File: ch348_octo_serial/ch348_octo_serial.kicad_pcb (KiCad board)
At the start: 2 copper layers, 88.9 x 88.9 mm, 73 parts, among them J1 USB_C_Receptacle_USB2.0, J10 Conn_01x07, J11 JLCPCB_3.5MM_SOCKET_C18166, J12 Conn_01x07, J13 JLCPCB_3.5MM_SOCKET_C18166, J14 Conn_01x07, J15 JLCPCB_3.5MM_SOCKET_C18166, J16 Conn_01x07, J17 JLCPCB_3.5MM_SOCKET_C18166, J18 Conn_01x07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

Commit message: ch348_octo_serial: fully routed, silk pending
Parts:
- moved D3 5.84 mm to (70.4, 80.0)
- moved D4 5.84 mm to (70.4, 87.6)
- moved R14 5.84 mm to (72.9, 80.0)
- moved R15 5.84 mm to (72.9, 87.6)
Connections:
- net Net-(C7-Pad1) renamed /RESET
- net Net-(C8-Pad1) renamed /XI
- net Net-(C9-Pad1) renamed /XO
- net Net-(D2-Pad1) renamed /ACT
- net Net-(R12-Pad2) renamed /TEST
- net Net-(R13-Pad2) renamed /CFG
- net Net-(R14-Pad1) renamed /RX_S
- net Net-(R15-Pad1) renamed /TX_S
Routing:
- net Vdrive: track 0.00 -> 533.0 mm, vias 0 -> 4
- net +3.3V: track 0.00 -> 198.4 mm, vias 0 -> 10
- net +5V: track 0.00 -> 135.3 mm, vias 0 -> 5
- net /Serial Connector 0/RTS: track 0.00 -> 86.6 mm, vias 0 -> 2
- net /Serial Connector 0/DTR: track 0.00 -> 86.1 mm, vias 0 -> 1
- net /Serial Connector 2/DTR: track 0.00 -> 84.9 mm, vias 0 -> 1
- net /Serial Connector 0/RXD: track 0.00 -> 81.9 mm, vias 0 -> 1
- net /Serial Connector 0/CTS: track 0.00 -> 80.3 mm, vias 0 -> 1
- net /Serial Connector 0/TXD: track 0.00 -> 77.8 mm, vias 0 -> 1
- net /Serial Connector 3/RXD: track 0.00 -> 70.9 mm, vias 0 -> 1
- net /Serial Connector 1/CTS: track 0.00 -> 70.4 mm, vias 0 -> 3
- net /Serial Connector 6/DTR: track 0.00 -> 68.5 mm, vias 0 -> 4
- net /Serial Connector 4/DTR: track 0.00 -> 67.7 mm, vias 0 -> 3
- net /Serial Connector 6/RTS: track 0.00 -> 67.1 mm
- net /Serial Connector 5/RXD: track 0.00 -> 65.9 mm, vias 0 -> 2
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- added copper zone on In2.Cu, net GND
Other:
- copper layers 2 -> 4

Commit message: ch348_octo_serial: Dec2022 as submitted
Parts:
- added H1: Front Octopus, ch348_octo_serial:octopus, F.Cu at (110.7, 75.7)
- added H2: Back Octopus, ch348_octo_serial:octopus_120, B.Cu at (107.6, 87.5)
- moved C1 16.8 mm to (94.5, 89.0), turned to 0 degrees
- moved R2 16.8 mm to (97.9, 88.6)
- moved R3 16.8 mm to (99.2, 88.6)
- moved VR1 16.8 mm to (96.1, 94.2)
- moved C4 16.7 mm to (92.2, 97.5), turned to 180 degrees
- moved J2 9.90 mm to (140.3, 56.5)
- moved J3 9.90 mm to (85.7, 56.5)
- moved J4 9.90 mm to (140.3, 111.1)
- moved J5 9.90 mm to (85.7, 111.1)
- moved C16 6.92 mm to (114.0, 107.1), turned to -90 degrees
- moved C22 5.32 mm to (71.5, 65.0), turned to 180 degrees
- moved C20 4.99 mm to (130.8, 45.0)
- moved C18 4.89 mm to (153.2, 102.4), turned to 0 degrees
- moved C24 4.44 mm to (94.2, 124.2), turned to -90 degrees
- moved R16 2.05 mm to (108.5, 118.4), turned to 180 degrees
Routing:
- net +3.3V: track 198.4 -> 189.3 mm
- net Vdrive: track 533.0 -> 541.7 mm
- net +5V: track 135.3 -> 128.6 mm
- net /Serial Connector 0/CTS: track 80.3 -> 76.9 mm
- net /Serial Connector 0/TXD: track 77.8 -> 79.7 mm
- net GND: track 64.1 -> 65.5 mm
- net /Serial Connector 0/RTS: track 86.6 -> 87.9 mm
- net /Serial Connector 1/TXD: track 57.9 -> 56.6 mm
- net /Serial Connector 0/RXD: track 81.9 -> 83.0 mm
- net /Serial Connector 6/CTS: track 56.4 -> 55.6 mm
- net /Serial Connector 1/CTS: track 70.4 -> 69.6 mm
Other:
- board text added: "+VIN-"
- board text added: "0"
- board text added: "1"
- board text added: "1.8V"
- board text added: "2"
- board text added: "2.5V"
- board text added: "3"
- board text added: "3.3V"
- board text added: "4"
- board text added: "5"
- board text added: "6"
- board text added: "7"
- board text added: "ACT"
- board text added: "CTS"
- board text added: "DTR"
- board text added: "GND"
- board text added: "RTS"
- board text added: "RX<"
- board text added: "RXD<"
- board text added: "TX>"
- board text added: "TXD>"
- board text added: "VCC"
- board text added: "VIN"
- board text added: "ch348 octo serial @TomKeddie Dec 2022"

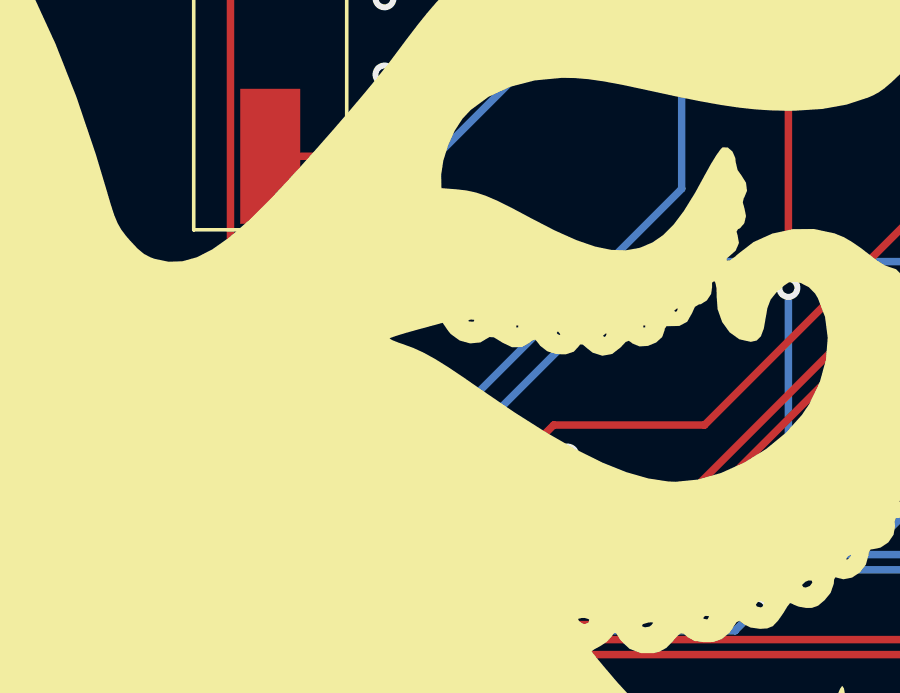
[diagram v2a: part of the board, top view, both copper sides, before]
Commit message: ch348_octo_serial: add pin 1 marking
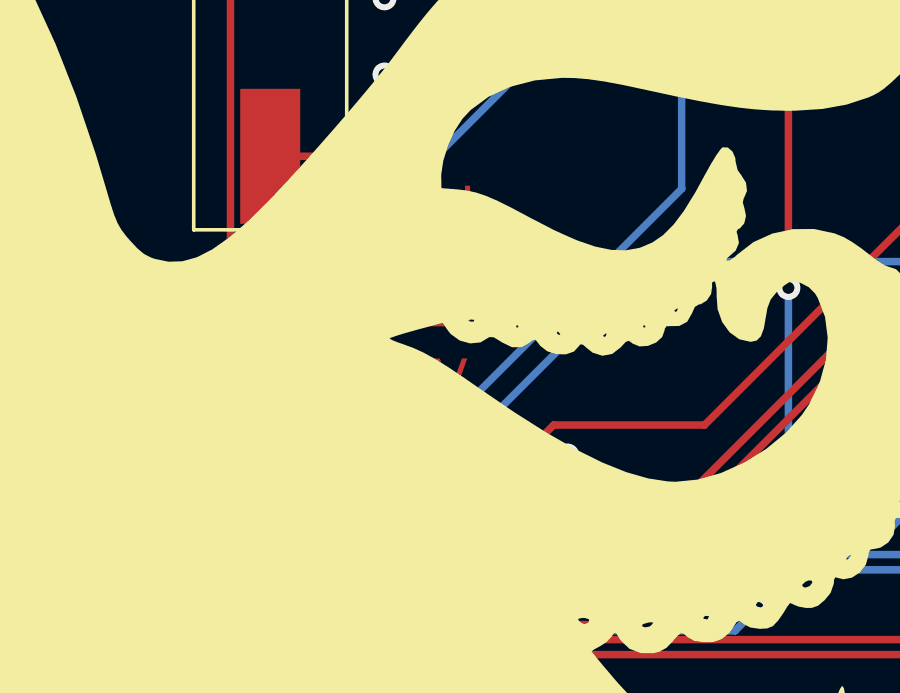
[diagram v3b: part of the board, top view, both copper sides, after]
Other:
- board text added: "< Pin 1"
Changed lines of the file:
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@@
   (gr_arc (start 73.66 128.27) (mid 70.067898 126.782102) (end 68.58 123.19) (layer "Edge.Cuts") (width 0.1))
   (gr_line (start 157.48 123.19) (end 157.48 44.45) (layer "Edge.Cuts") (width 0.1))
+  (gr_text "< Pin 1" (at 119 66 90) (layer "F.Cu")
+    (effects (font (size 1.5 1.5) (thickness 0.3)) (justify right))
+  )
   (gr_text "RXD<" (at 152.654 115.57) (layer "F.SilkS")
     (effects (font (size 1.9 1.9) (thickness 0.4)) (justify right))
